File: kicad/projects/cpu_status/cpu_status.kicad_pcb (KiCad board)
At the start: 2 copper layers, 203.2 x 97.8 mm, 103 parts, among them J1 Control_signal_backplane, J2 Aux_connection, J3 Bus_connection, J4 MAR_content_in, U1 74HC245, U2 74HC245, U3 74HC245, U4 74HC245, U5 74HC245, U6 74HC245, U7 74HC245, U8 74HC245, U9 74HC126

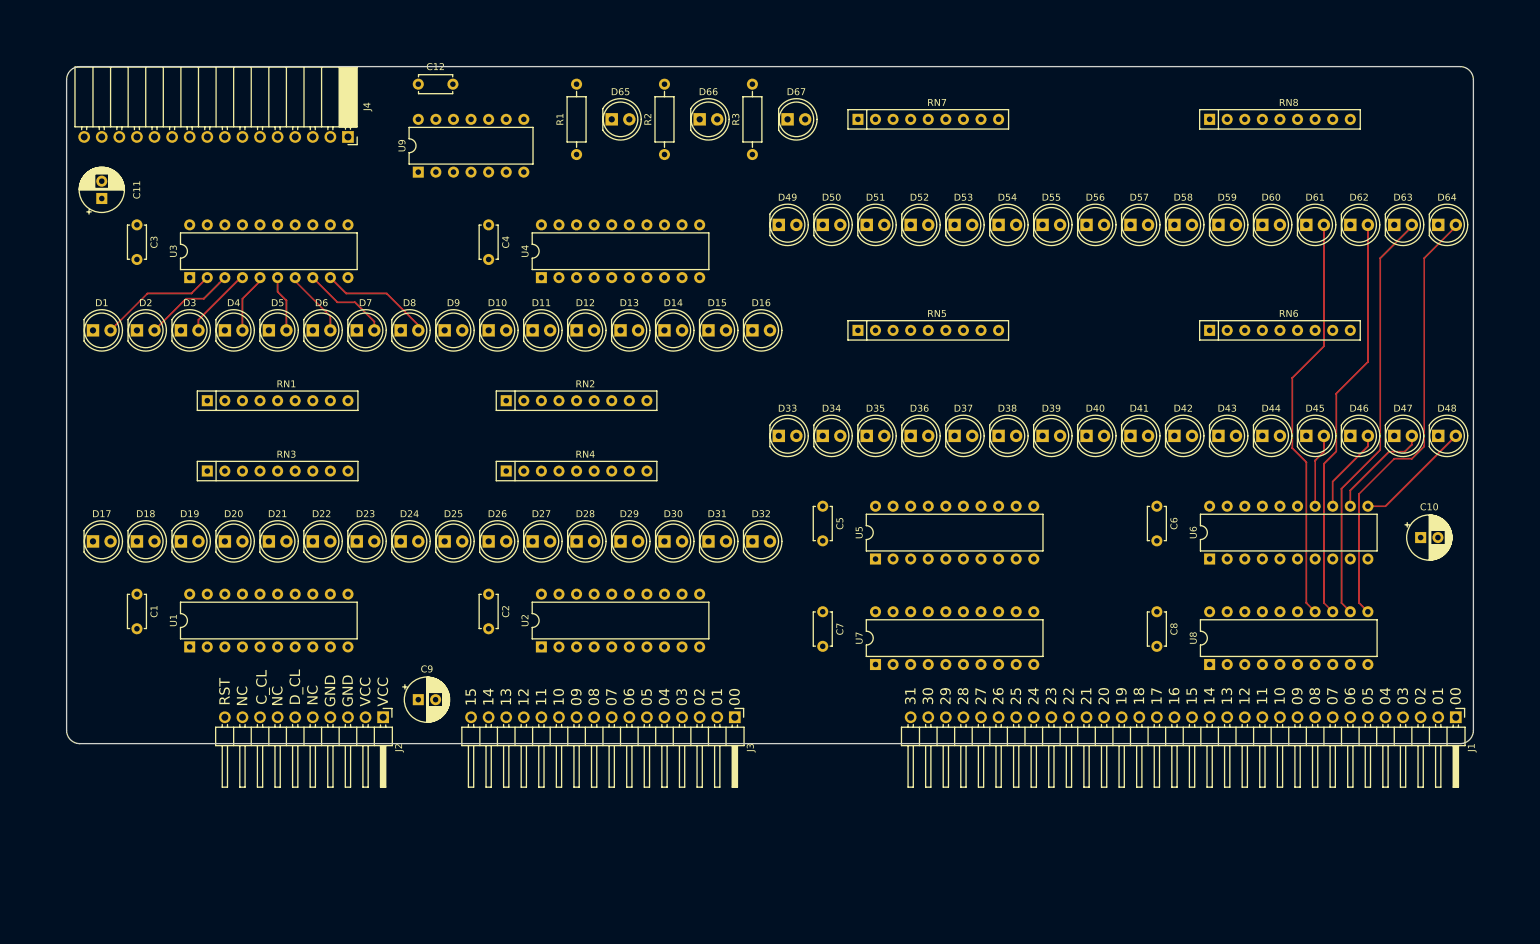
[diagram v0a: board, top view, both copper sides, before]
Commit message: Bit of wiring on the CPU status board.
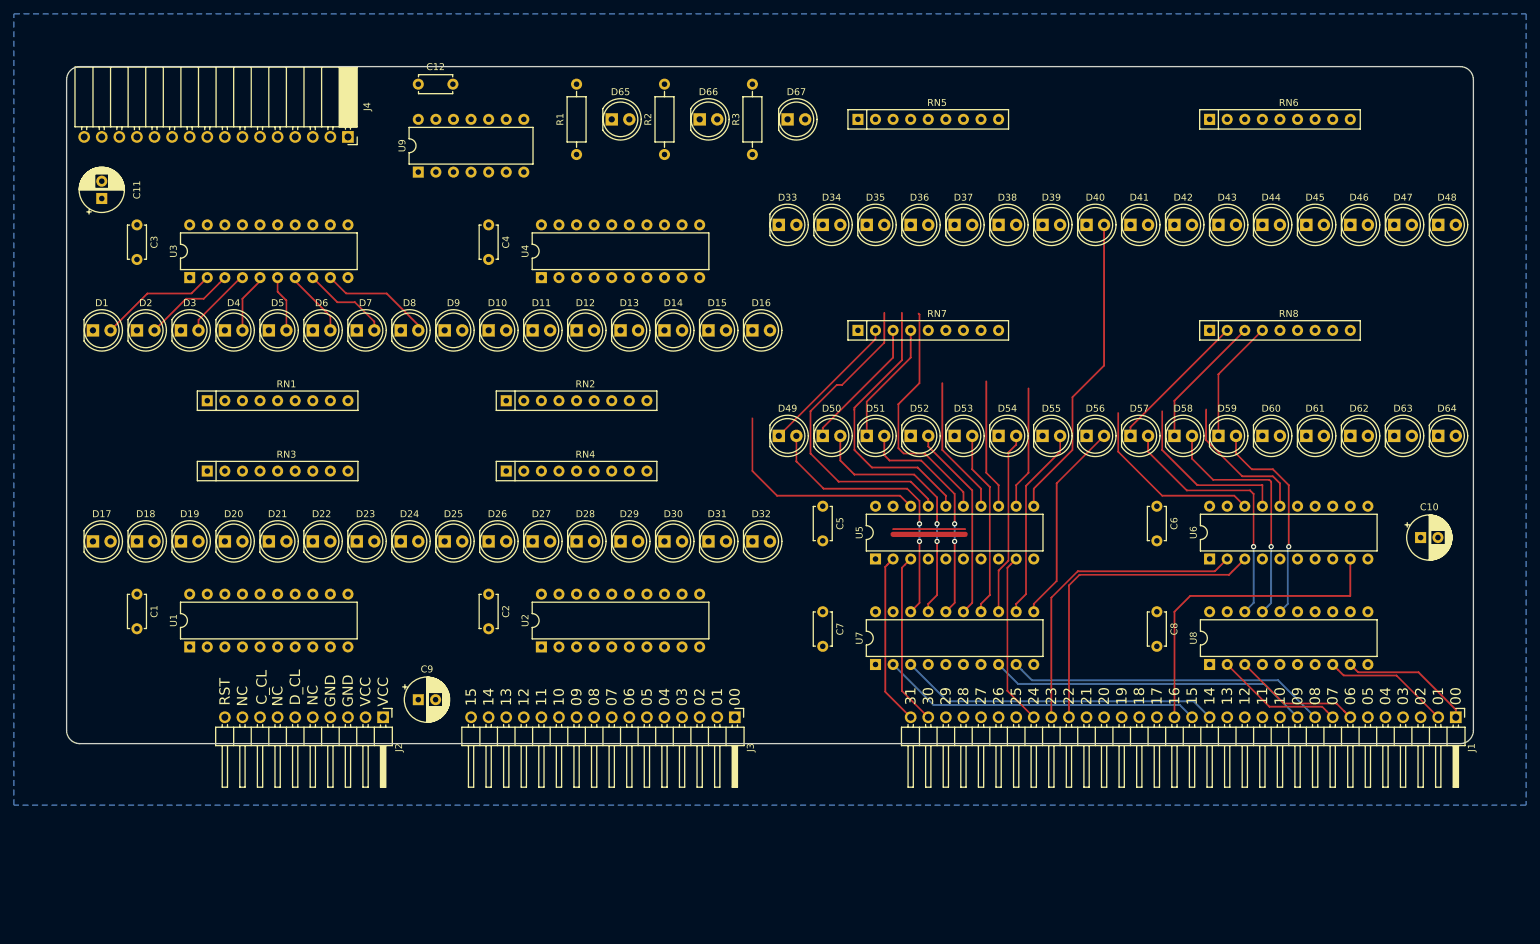
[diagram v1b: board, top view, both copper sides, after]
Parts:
- moved D33 30.5 mm to (153.7, 73.7)
- moved D34 30.5 mm to (160.0, 73.7)
- moved D35 30.5 mm to (166.4, 73.7)
- moved D36 30.5 mm to (172.7, 73.7)
- moved D37 30.5 mm to (179.1, 73.7)
- moved D38 30.5 mm to (185.4, 73.7)
- moved D39 30.5 mm to (191.8, 73.7)
- moved D40 30.5 mm to (198.1, 73.7)
- moved D41 30.5 mm to (204.5, 73.7)
- moved D42 30.5 mm to (210.8, 73.7)
- moved D43 30.5 mm to (217.2, 73.7)
- moved D44 30.5 mm to (223.5, 73.7)
- moved D45 30.5 mm to (229.9, 73.7)
- moved D46 30.5 mm to (236.2, 73.7)
- moved D47 30.5 mm to (242.6, 73.7)
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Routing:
- net Net-(D64-Pad2): track 63.4 -> 0.00 mm
- net Net-(D63-Pad2): track 60.4 -> 0.00 mm
- net Net-(D61-Pad2): track 59.1 -> 0.00 mm
- net Net-(D62-Pad2): track 59.0 -> 0.00 mm
- net /ALU_M: track 0.00 -> 46.9 mm
- net /ALU_ST_FL: track 0.00 -> 46.3 mm
- net /ALU_S3: track 0.00 -> 46.3 mm
- net /ALU_S2: track 0.00 -> 46.3 mm
- net /ALU_ST_RS: track 0.00 -> 46.3 mm
- net /SP_OUT: track 0.00 -> 46.0 mm
- net Net-(D34-Pad2): track 0.00 -> 46.0 mm
- net /PC_IN: track 0.00 -> 45.0 mm
- net Net-(D40-Pad2): track 0.00 -> 44.8 mm
- net Net-(D49-Pad2): track 0.00 -> 40.4 mm, vias 0 -> 2
- net Net-(D35-Pad2): track 0.00 -> 40.1 mm
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- added copper zone on B.Cu, net GND

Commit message: Added power port and LED control to status board.
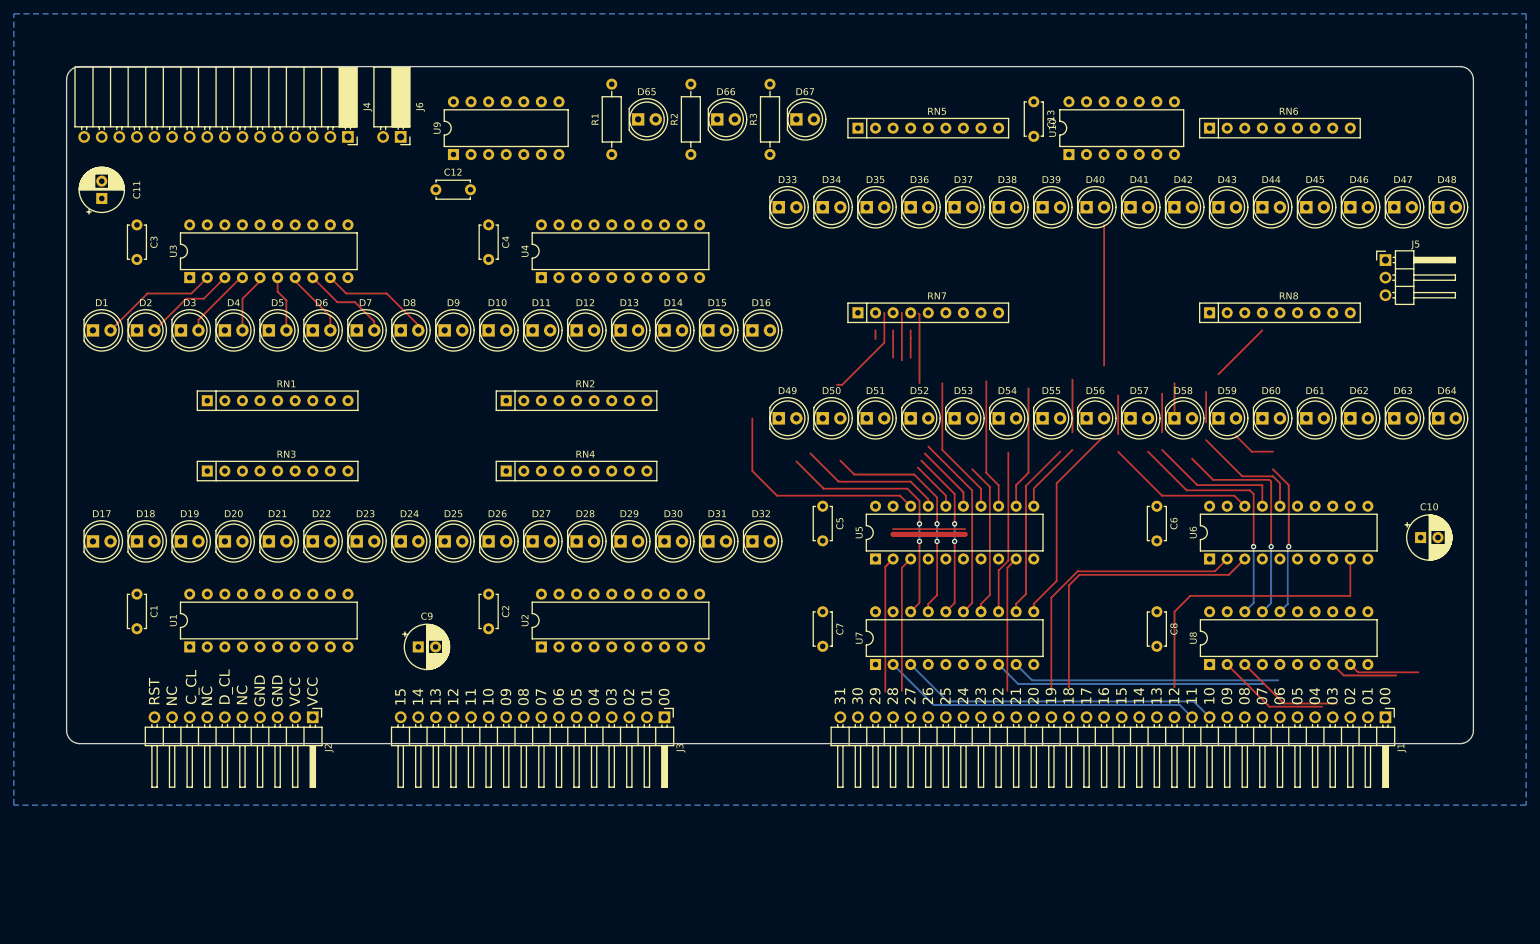
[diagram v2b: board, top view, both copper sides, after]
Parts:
- added C13: 0.1uF, Capacitor_THT:C_Disc_D4.7mm_W2.5mm_P5.00mm, F.Cu at (190.5, 55.9)
- added J5: Conn_01x03_Male, Connector_PinHeader_2.54mm:PinHeader_1x03_P2.54mm_Horizontal, F.Cu at (241.3, 78.7)
- added J6: Conn_01x02_Female, Connector_PinSocket_2.54mm:PinSocket_1x02_P2.54mm_Horizontal, F.Cu at (99.1, 61.0)
- added U10: 74HC04, Package_DIP:DIP-14_W7.62mm, F.Cu at (195.6, 63.5)
- moved C12 15.5 mm to (104.1, 68.6)
- moved J1 10.2 mm to (241.3, 144.8)
- moved J2 10.2 mm to (86.4, 144.8)
- moved J3 10.2 mm to (137.2, 144.8)
- moved C9 7.62 mm to (101.6, 134.6)
- moved U9 5.68 mm to (106.7, 63.5)
- moved R1 5.08 mm to (129.5, 63.5)
- moved D65 3.81 mm to (133.3, 58.4)
- moved R2 3.81 mm to (141.0, 63.5)
- moved D49 2.54 mm to (153.7, 101.6)
- moved D50 2.54 mm to (160.0, 101.6)
- moved D51 2.54 mm to (166.4, 101.6)
- moved D52 2.54 mm to (172.7, 101.6)
- moved D53 2.54 mm to (179.1, 101.6)
- moved D54 2.54 mm to (185.4, 101.6)
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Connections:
- U9 pad 1: VCC -> Net-(U10-Pad2)
- U9 pad 10: VCC -> Net-(U10-Pad2)
- U9 pad 4: VCC -> Net-(U10-Pad2)
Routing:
- net Net-(D35-Pad2): track 40.1 -> 14.1 mm
- net Net-(D49-Pad1): track 21.3 -> 0.00 mm
- net Net-(D57-Pad1): track 21.0 -> 0.00 mm
- net Net-(D50-Pad1): track 19.4 -> 0.00 mm
- net Net-(D36-Pad2): track 34.8 -> 20.0 mm
- net Net-(D58-Pad1): track 19.4 -> 5.08 mm
- net Net-(D34-Pad2): track 46.0 -> 34.5 mm
- net Net-(D51-Pad1): track 17.9 -> 7.87 mm
- net Net-(D59-Pad1): track 17.9 -> 8.98 mm
- net /ACC_IN: track 19.0 -> 10.3 mm
- net /ACC_OUT: track 18.4 -> 9.86 mm
- net Net-(D51-Pad2): track 32.8 -> 24.4 mm
- net /ALU_ST_RS: track 46.3 -> 38.8 mm
- net /ALU_ST_FL: track 46.3 -> 39.5 mm
- net Net-(D40-Pad2): track 44.8 -> 38.4 mm
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
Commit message: Finish wiring on CPU Status.
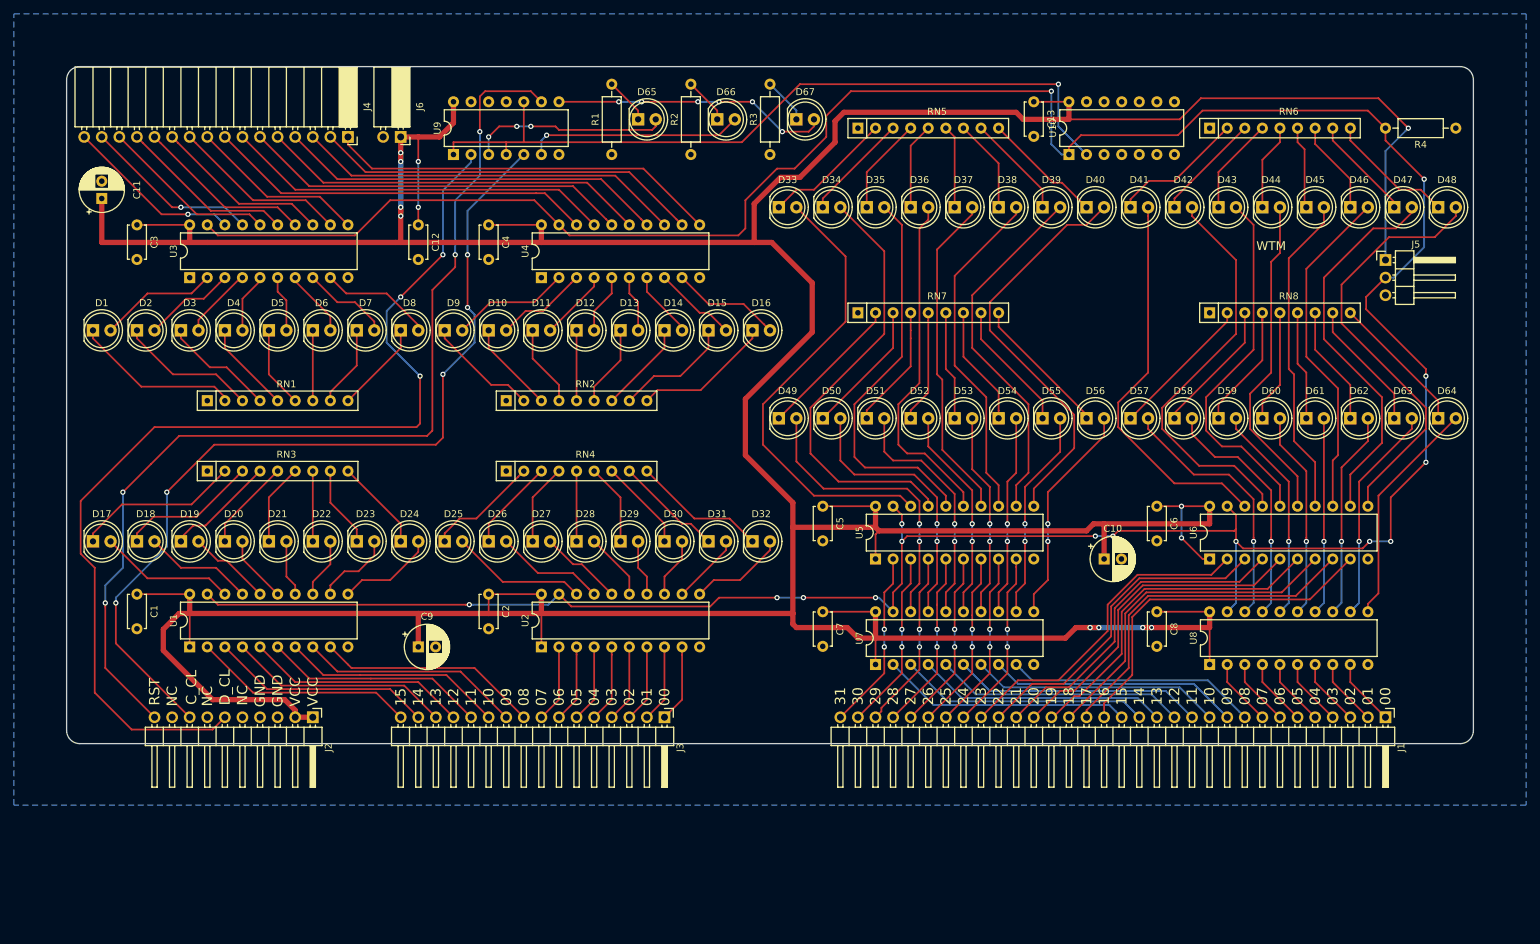
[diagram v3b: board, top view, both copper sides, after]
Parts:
- added R4: 10K, Resistor_THT:R_Axial_DIN0207_L6.3mm_D2.5mm_P10.16mm_Horizontal, F.Cu at (251.5, 59.7)
- D1, D10, D11, D12, D13, D14, D15, D16, D17, D18, D19, D2, D20, D21, D22, D23, D24, D25, D26, D27, D28, D29, D3, D30, D31, D32, D33, D34, D35, D36, D37, D38, D39, D4, D40, D41, D42, D43, D44, D45, D46, D47, D48, D49, D5, D50, D51, D52, D53, D54, D55, D56, D57, D58, D59, D6, D60, D61, D62, D63, D64, D65, D66, D67, D7, D8, D9: footprint LED_THT:LED_D5.0mm -> sixteen-bit-computer:LED_D5.0mm
- moved C10 45.8 mm to (200.7, 121.9)
- moved C12 5.68 mm to (101.6, 73.7), turned to 270 degrees
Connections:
- U1 pad 19: GND -> /LED_CONTROL
- U2 pad 19: GND -> /LED_CONTROL
- U3 pad 19: GND -> /LED_CONTROL
- U4 pad 19: GND -> /LED_CONTROL
- U5 pad 19: GND -> /LED_CONTROL
- U6 pad 19: GND -> /LED_CONTROL
- U7 pad 19: GND -> /LED_CONTROL
- U8 pad 19: GND -> /LED_CONTROL
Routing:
- net VCC: track 0.00 -> 723.5 mm, vias 0 -> 13
- net /LED_CONTROL: track 0.00 -> 479.4 mm, vias 0 -> 15
- net /DATA_CLK: track 0.00 -> 149.8 mm, vias 0 -> 3
- net /RESET: track 0.00 -> 145.8 mm, vias 0 -> 4
- net /CTL_CLK: track 0.00 -> 129.7 mm, vias 0 -> 5
- net Net-(U10-Pad2): track 0.00 -> 112.1 mm, vias 0 -> 1
- net Net-(D48-Pad2): track 0.00 -> 62.4 mm
- net /MAR_00: track 0.00 -> 56.7 mm
- net /MAR_03: track 0.00 -> 56.1 mm
- net /MAR_07: track 0.00 -> 56.1 mm
- net /MAR_04: track 0.00 -> 56.1 mm
- net /MAR_02: track 0.00 -> 56.1 mm
- net /MAR_06: track 0.00 -> 56.1 mm
- net /MAR_05: track 0.00 -> 56.1 mm
- net /MAR_01: track 0.00 -> 56.1 mm
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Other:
- board text added: "WTM"

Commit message: Labelling on CPU status.
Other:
- board text added: "0"
- board text added: "1"
- board text added: "10"
- board text added: "1024"
- board text added: "11"
- board text added: "12"
- board text added: "128"
- board text added: "13"
- board text added: "14"
- board text added: "15"
- board text added: "16384"
- board text added: "2"
- board text added: "2048"
- board text added: "256"
- board text added: "3"
- board text added: "32"
- board text added: "32768"
- board text added: "4"
- board text added: "4096"
- board text added: "5"
- board text added: "512"
- board text added: "6"
- board text added: "64"
- board text added: "65536"
- board text added: "7"
- board text added: "8"
- board text added: "8192"
- board text added: "9"
- board text added: "A IN"
- board text added: "A OUT"
- board text added: "ACC IN"
- board text added: "ACC OUT"
- board text added: "ADDRESS"
- board text added: "ALU A BUS"
- board text added: "ALU CARRY"
- board text added: "ALU M"
- board text added: "ALU OUT"
- board text added: "ALU S0"
- board text added: "ALU S1"
- board text added: "ALU S2"
- board text added: "ALU S3"
- board text added: "ALU ST FL"
- board text added: "ALU ST RS"
- board text added: "B IN"
- board text added: "B OUT"
- board text added: "C IN"
- board text added: "C OUT"
- board text added: "CTL CLK"
- board text added: "CU ST RST"
- board text added: "CU29"
- board text added: "CU30"
- board text added: "CU31"
- board text added: "DATA"
- board text added: "DATA CLK"
- board text added: "GND"
- board text added: "HALT"
- board text added: "IR IN"
- board text added: "MAR IN"
- board text added: "PC COUNT"
- board text added: "PC IN"
- board text added: "PC OUT"
- board text added: "RESET"
- board text added: "RFM"
- board text added: "SP IN"
- board text added: "SP OUT"
- board text added: "VCC"
- board text added: "~LED OE"

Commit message: Finish off CPU status.
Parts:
- moved C1 2.54 mm to (61.0, 129.5)
- moved C2 2.54 mm to (111.8, 129.5)
- moved U1 2.54 mm to (68.6, 137.2)
- moved U2 2.54 mm to (119.4, 137.2)
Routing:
- net VCC: track 723.5 -> 715.3 mm
- net Net-(D32-Pad2): track 14.1 -> 16.6 mm
- net Net-(D19-Pad2): track 12.0 -> 14.6 mm
- net Net-(D30-Pad2): track 8.67 -> 11.2 mm
- net Net-(D29-Pad2): track 8.15 -> 10.7 mm
- net Net-(D28-Pad2): track 9.72 -> 12.3 mm
- net Net-(D27-Pad2): track 12.0 -> 14.6 mm
- net Net-(D24-Pad2): track 14.2 -> 16.7 mm
- net Net-(D23-Pad2): track 11.4 -> 14.0 mm
- net Net-(D22-Pad2): track 8.67 -> 11.2 mm
- net Net-(D21-Pad2): track 8.15 -> 10.7 mm
- net Net-(D20-Pad2): track 9.72 -> 12.3 mm
- net Net-(D18-Pad2): track 15.9 -> 18.4 mm
- net Net-(D17-Pad2): track 19.7 -> 22.2 mm
- net /BUS_07: track 11.2 -> 8.67 mm
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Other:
- board text added: "16"
- board text added: "17"
- board text added: "18"
- board text added: "19"
- board text added: "20"
- board text added: "21"
- board text added: "22"
- board text added: "23"
- board text added: "24"
- board text added: "25"
- board text added: "26"
- board text added: "27"
- board text added: "28"
- board text added: "29"
- board text added: "30"
- board text added: "31"
